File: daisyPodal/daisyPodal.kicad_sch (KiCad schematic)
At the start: 50 parts, among them J1 Guitar in, J2 fsw pin 1, J3 fsw pin 2, J4 fsw pin 4, J5 fsw pin 5, J6 fsw pin 6, J7 Left out, J8 Right out, J9 fsw pin 3, SW1 Switch 1, SW2 Switch 2, SW3 RotaryEncoder_Switch, U1 TL074, U2 L78L05_TO92

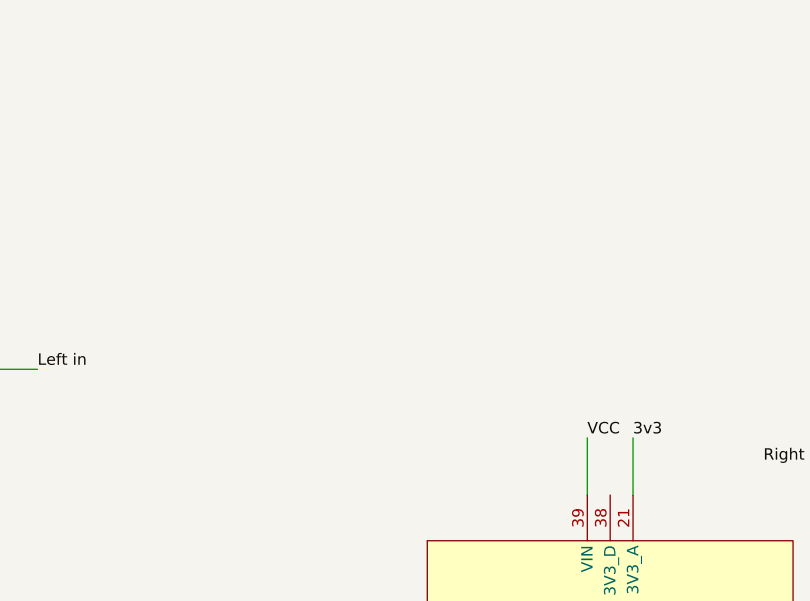
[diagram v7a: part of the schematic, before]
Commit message: Terminate unused op-amp
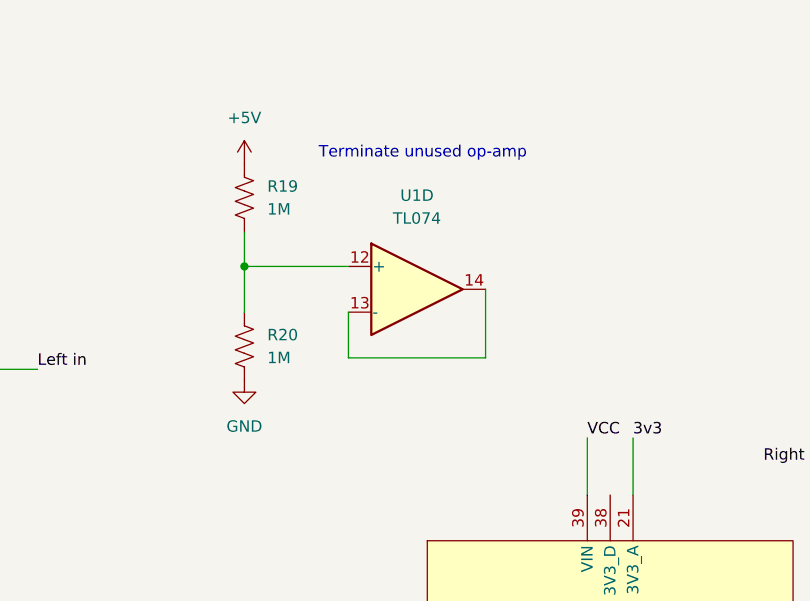
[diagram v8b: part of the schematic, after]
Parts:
- added R19, R20: 1M, Resistor_THT:R_Axial_DIN0207_L6.3mm_D2.5mm_P10.16mm_Horizontal, symbol Device:R_US
- added unit 4 of U1
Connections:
- net +5V: now also R19.1
- net GND: now also R20.2
- new net: R19.2, R20.1, U1.12 (+)
- new net: U1.13 (-), U1.14
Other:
- note added: "Terminate unused op-amp"
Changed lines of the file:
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@@
   (junction (at 259.461 66.421) (diameter 0) (color 0 0 0 0)
   )
+  (junction (at 121.92 41.91) (diameter 0) (color 0 0 0 0)
+  )
   (junction (at 205.867 32.004) (diameter 0) (color 0 0 0 0)
   )
@@
     (stroke (width 0) (type default))
   )
+  (wire (pts (xy 133.477 46.99) (xy 133.477 52.07))
+    (stroke (width 0) (type default))
+  )
   (wire (pts (xy 233.934 66.421) (xy 233.934 74.041))
     (stroke (width 0) (type default))
@@
     (stroke (width 0) (type default))
   )
+  (wire (pts (xy 121.92 38.1) (xy 121.92 41.91))
+    (stroke (width 0) (type default))
+  )
   (wire (pts (xy 267.843 38.354) (xy 267.843 34.544))
     (stroke (width 0) (type default))
@@
     (stroke (width 0) (type default))
   )
+  (wire (pts (xy 133.477 41.91) (xy 121.92 41.91))
+    (stroke (width 0) (type default))
+  )
   (wire (pts (xy 160.02 143.51) (xy 160.02 152.4))
     (stroke (width 0) (type default))
@@
     (stroke (width 0) (type default))
   )
+  (wire (pts (xy 133.477 52.07) (xy 148.717 52.07))
+    (stroke (width 0) (type default))
+  )
   (wire (pts (xy 266.192 34.544) (xy 267.843 34.544))
     (stroke (width 0) (type default))
@@
     (stroke (width 0) (type default))
   )
+  (wire (pts (xy 121.92 41.91) (xy 121.92 46.99))
+    (stroke (width 0) (type default))
+  )
   (wire (pts (xy 259.461 70.231) (xy 259.461 66.421))
     (stroke (width 0) (type default))
@@
   (wire (pts (xy 18.415 161.29) (xy 36.195 161.29))
     (stroke (width 0) (type default))
+  )
+  (wire (pts (xy 148.717 52.07) (xy 148.717 44.45))
+    (stroke (width 0) (type default))
+  )
+  (text "Terminate unused op-amp" (at 130.175 30.099 0)
+    (effects (font (size 1.27 1.27)) (justify left bottom))
   )
   (label "VCC" (at 160.02 60.96 0) (fields_autoplaced)
@@
     )
   )
+  (symbol (lib_id "power:+5V") (at 121.92 30.48 0) (unit 1)
+    (in_bom yes) (on_board yes) (dnp no) (fields_autoplaced)
+    (property "Reference" "#PWR029" (at 121.92 34.29 0)
+      (effects (font (size 1.27 1.27)) hide)
+    )
+    (property "Value" "+5V" (at 121.92 25.4 0)
+      (effects (font (size 1.27 1.27)))
+    )
+    (property "Footprint" "" (at 121.92 30.48 0)
+      (effects (font (size 1.27 1.27)) hide)
+    )
+    (property "Datasheet" "" (at 121.92 30.48 0)
+      (effects (font (size 1.27 1.27)) hide)
+    )
+    (pin "1")
+    (instances
+      (project "daisyPodal"
+        (path "/12e895f7-e5ae-4934-aed6-e6e04c63dd03"
+          (reference "#PWR029") (unit 1)
+        )
+      )
+    )
+  )
   (symbol (lib_id "power:GND") (at 214.122 41.783 0) (unit 1)
     (in_bom yes) (on_board yes) (dnp no) (fields_autoplaced)
@@
         (path "/12e895f7-e5ae-4934-aed6-e6e04c63dd03"
           (reference "#PWR024") (unit 1)
+        )
+      )
+    )
+  )
+  (symbol (lib_id "Amplifier_Operational:TL074") (at 141.097 44.45 0) (unit 4)
+    (in_bom yes) (on_board yes) (dnp no) (fields_autoplaced)
+    (property "Reference" "U1" (at 141.097 34.036 0)
+      (effects (font (size 1.27 1.27)))
+    )
+    (property "Value" "TL074" (at 141.097 36.576 0)
+      (effects (font (size 1.27 1.27)))
+    )
+    (property "Footprint" "" (at 139.827 41.91 0)
+      (effects (font (size 1.27 1.27)) hide)
+    )
+    (property "Datasheet" "http://www.ti.com/lit/ds/symlink/tl071.pdf" (at 142.367 39.37 0)
+      (effects (font (size 1.27 1.27)) hide)
+    )
+    (pin "1")
+    (pin "12")
+    (pin "10")
+    (pin "2")
+    (pin "6")
+    (pin "13")
+    (pin "5")
+    (pin "9")
+    (pin "14")
+    (pin "11")
+    (pin "3")
+    (pin "8")
+    (pin "7")
+    (pin "4")
+    (instances
+      (project "daisyPodal"
+        (path "/12e895f7-e5ae-4934-aed6-e6e04c63dd03"
+          (reference "U1") (unit 4)
         )
       )
@@
     )
   )
+  (symbol (lib_id "power:GND") (at 121.92 54.61 0) (unit 1)
+    (in_bom yes) (on_board yes) (dnp no) (fields_autoplaced)
+    (property "Reference" "#PWR030" (at 121.92 60.96 0)
+      (effects (font (size 1.27 1.27)) hide)
+    )
+    (property "Value" "GND" (at 121.92 59.69 0)
+      (effects (font (size 1.27 1.27)))
+    )
+    (property "Footprint" "" (at 121.92 54.61 0)
+      (effects (font (size 1.27 1.27)) hide)
+    )
+    (property "Datasheet" "" (at 121.92 54.61 0)
+      (effects (font (size 1.27 1.27)) hide)
+    )
+    (pin "1")
+    (instances
+      (project "daisyPodal"
+        (path "/12e895f7-e5ae-4934-aed6-e6e04c63dd03"
+          (reference "#PWR030") (unit 1)
+        )
+      )
+    )
+  )
   (symbol (lib_id "Device:R_US") (at 40.767 59.69 0) (unit 1)
     (in_bom yes) (on_board yes) (dnp no) (fields_autoplaced)
@@
         (path "/12e895f7-e5ae-4934-aed6-e6e04c63dd03"
           (reference "J2") (unit 1)
+        )
+      )
+    )
+  )
+  (symbol (lib_id "Device:R_US") (at 121.92 50.8 0) (unit 1)
+    (in_bom yes) (on_board yes) (dnp no) (fields_autoplaced)
+    (property "Reference" "R20" (at 124.46 49.53 0)
+      (effects (font (size 1.27 1.27)) (justify left))
+    )
+    (property "Value" "1M" (at 124.46 52.07 0)
+      (effects (font (size 1.27 1.27)) (justify left))
+    )
+    (property "Footprint" "Resistor_THT:R_Axial_DIN0207_L6.3mm_D2.5mm_P10.16mm_Horizontal" (at 122.936 51.054 90)
+      (effects (font (size 1.27 1.27)) hide)
+    )
+    (property "Datasheet" "~" (at 121.92 50.8 0)
+      (effects (font (size 1.27 1.27)) hide)
+    )
+    (pin "1")
+    (pin "2")
+    (instances
+      (project "daisyPodal"
+        (path "/12e895f7-e5ae-4934-aed6-e6e04c63dd03"
+          (reference "R20") (unit 1)
         )
       )
@@
         )
       )
+    )
+  )
+  (symbol (lib_id "Device:R_US") (at 121.92 34.29 0) (unit 1)
+    (in_bom yes) (on_board yes) (dnp no) (fields_autoplaced)
+    (property "Reference" "R19" (at 124.46 33.02 0)
+      (effects (font (size 1.27 1.27)) (justify left))
+    )
+    (property "Value" "1M" (at 124.46 35.56 0)
+      (effects (font (size 1.27 1.27)) (justify left))
+    )
+    (property "Footprint" "Resistor_THT:R_Axial_DIN0207_L6.3mm_D2.5mm_P10.16mm_Horizontal" (at 122.936 34.544 90)
+      (effects (font (size 1.27 1.27)) hide)
+    )
+    (property "Datasheet" "~" (at 121.92 34.29 0)
+      (effects (font (size 1.27 1.27)) hide)
+    )
+    (pin "1")
+    (pin "2")
+    (instances
+      (project "daisyPodal"
+        (path "/12e895f7-e5ae-4934-aed6-e6e04c63dd03"
+          (reference "R19") (unit 1)
+        )
+      )
